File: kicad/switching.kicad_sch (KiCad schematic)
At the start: 7 parts

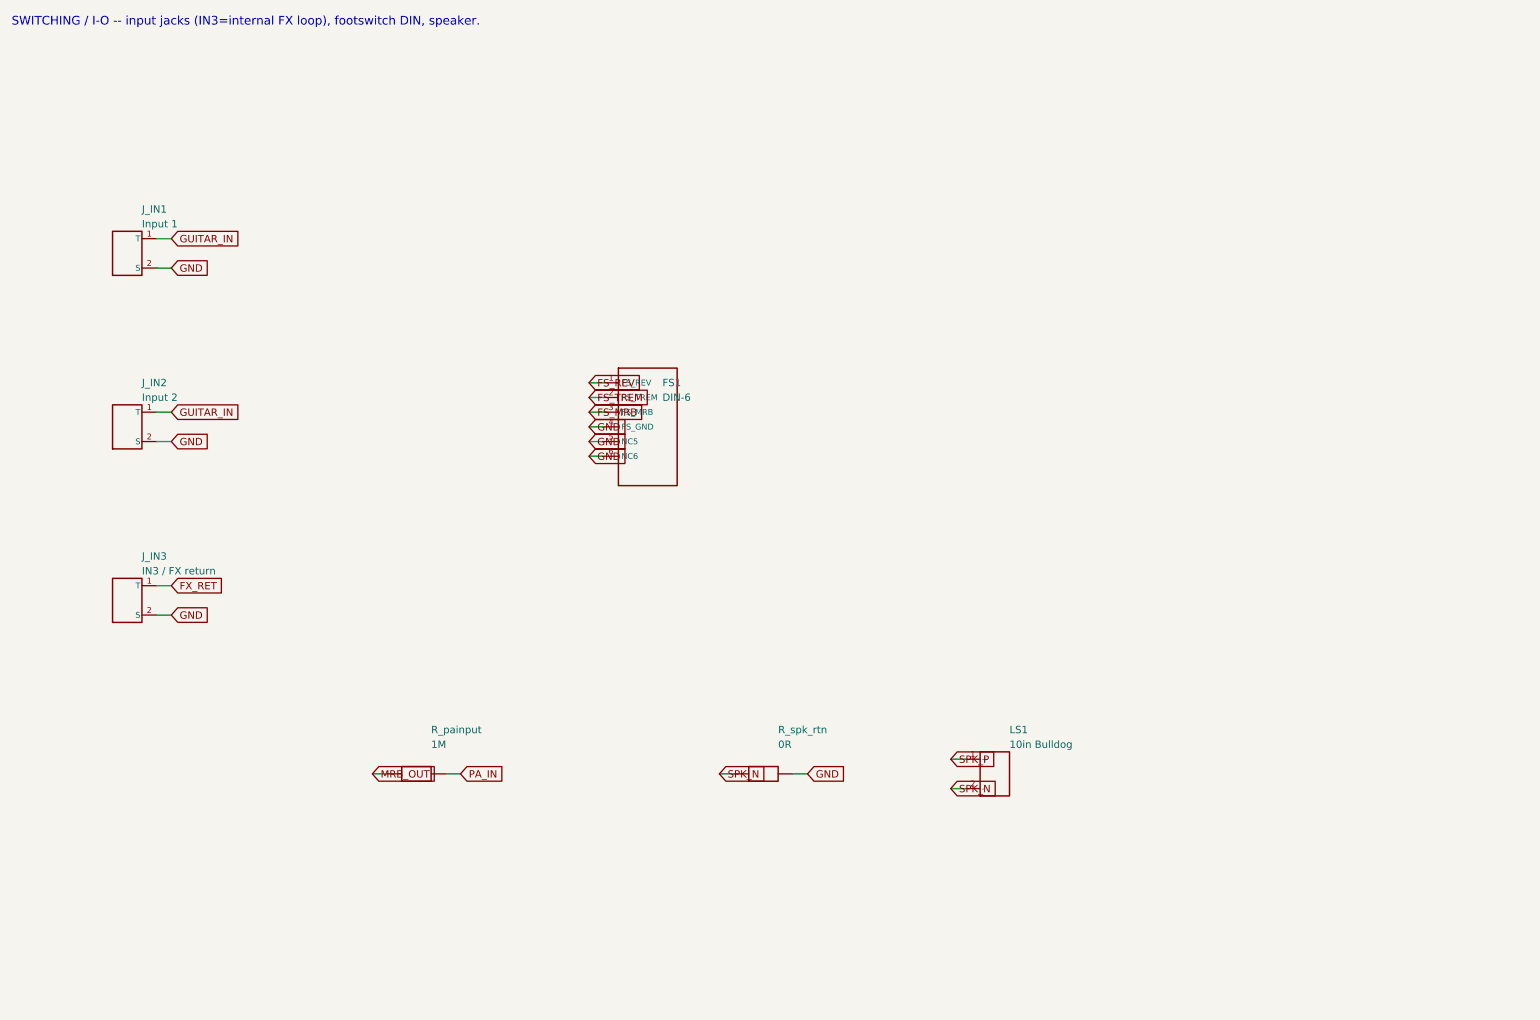
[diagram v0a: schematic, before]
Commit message: Schematic passes KiCad 8 ERC (0 violations); add op-amp mid-rail bias
Installed KiCad 8.0.9 and ran a real Electrical Rules Check on the generated
hierarchy. Drove it to 0 violations:
- snapped every pin/wire endpoint to the 1.27 mm connection grid (was 338
  endpoint_off_grid violations)
- gave the footswitch lines FS_REV/FS_TREM/FS_MRB a real second endpoint via
  100k control pulldowns on the reverb/tremolo/mrb sheets (was 3 dangling labels)

Also made the single-supply TL072 stages electrically real: added a mid-rail
VBIAS network (R_vb1/R_vb2 + C_vb on the Power Supply sheet) and referenced the
reverb driver and tremolo LFO inputs/gain-returns to VBIAS instead of GND
(design addition, flagged in the sheet notes).

Result: kicad-cli 8.0.9 sch erc -> 0 violations; netlist 102 components, 58
nets, 0 unconnected pins; VBIAS spans 10 nodes. Updated SCHEMATIC-BUILD.md,
kicad/README.md, CHANGELOG.md.

https://claude.ai/code/session_01PkrfUi9tvZfLvudJ7h23qD
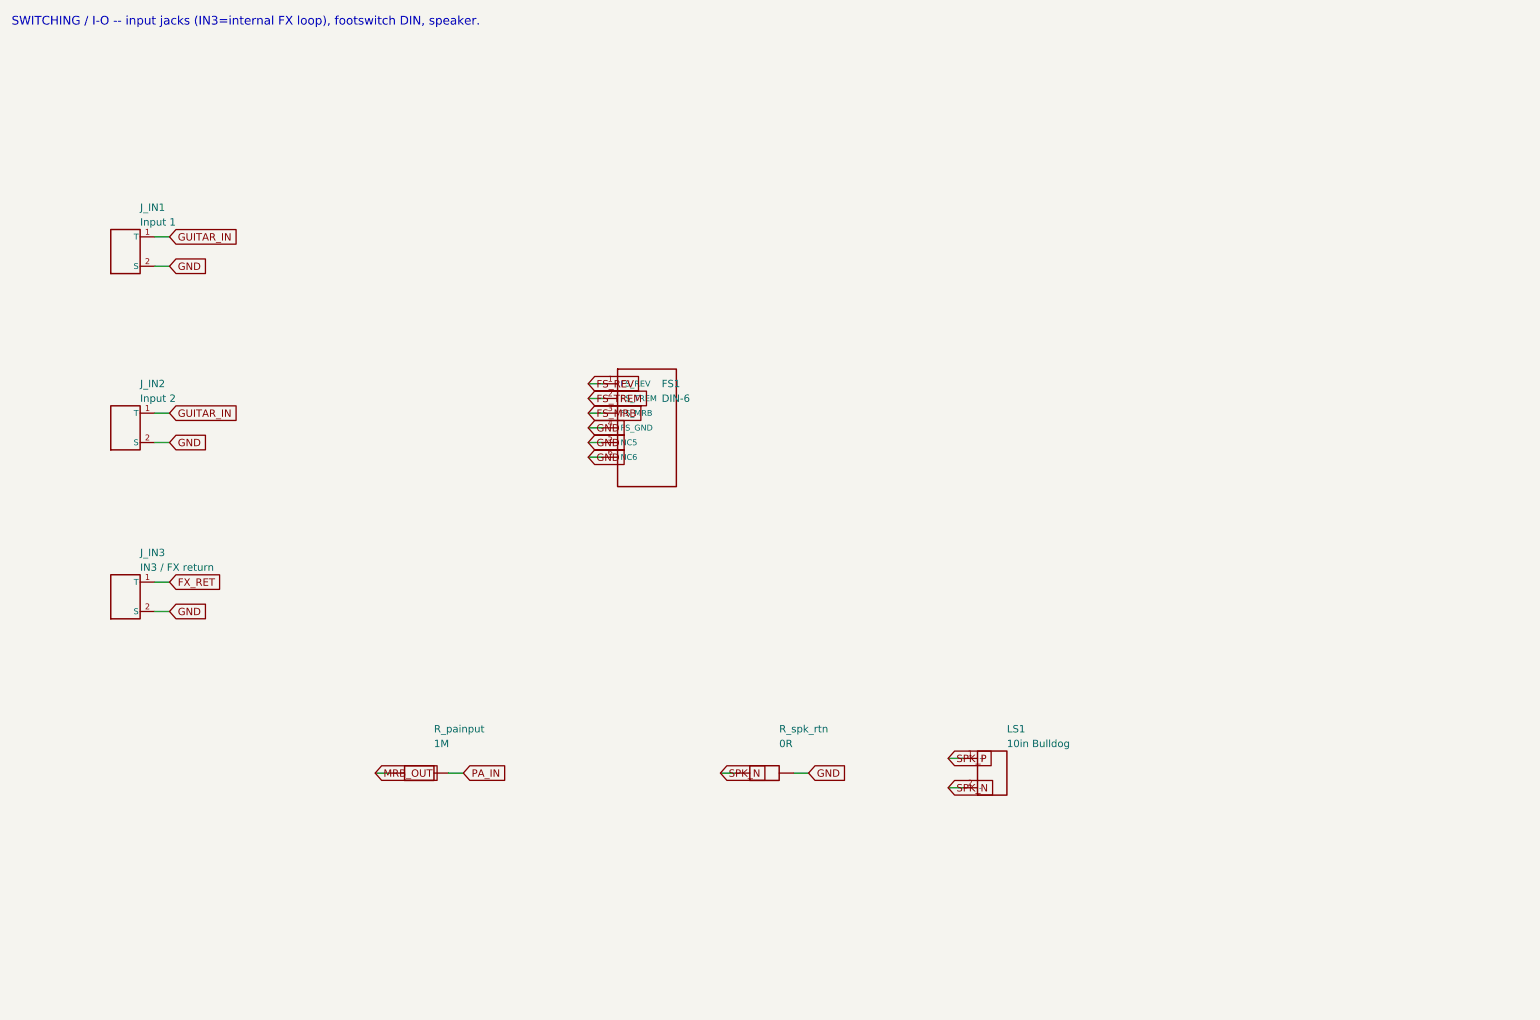
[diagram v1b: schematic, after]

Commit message: Generate auto-placed PCB (102 footprints, GND pour, board outline)
Build cambridge_reverb.kicad_pcb from the schematic via kicad/gen/gen_pcb.py
(KiCad 8 pcbnew API): assign a THT footprint to every component (standard libs
for generics + the project footprints for VTL5C1 and the 1H toroid), place all
102 footprints (off-board connectors on a bottom wiring-edge strip, toroid in a
reserved spot), assign all 58 nets to pads, draw a 190x115 mm Edge.Cuts outline,
and pour a bottom-layer GND plane. Footprint assignments also carry into the
schematic symbols.

The board opens in KiCad and the ratsnest matches the ERC-clean schematic. It is
placed but NOT routed: kicad-cli pcb drc is dominated by 130 unconnected
(unrouted signal nets; GND is poured) plus cosmetic silk/courtyard overlaps from
dense auto-placement at chassis size -- documented in kicad/PCB-NOTES.md with the
remaining hand-work (placement into floor-plan zones, routing, DRC-to-zero,
Gerbers). Net classes (Default/Power/HighCurrent) carry over for routing.

Also: schematic resistor footprint switched to the compact vertical variant;
gitignore DRC/ERC .rpt reports.

https://claude.ai/code/session_01PkrfUi9tvZfLvudJ7h23qD
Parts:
- FS1: footprint (none) -> Connector_PinHeader_2.54mm:PinHeader_1x06_P2.54mm_Vertical
- J_IN1, J_IN2, J_IN3, LS1: footprint (none) -> Connector_PinHeader_2.54mm:PinHeader_1x02_P2.54mm_Vertical
- R_painput, R_spk_rtn: footprint (none) -> Resistor_THT:R_Axial_DIN0207_L6.3mm_D2.5mm_P5.08mm_Vertical
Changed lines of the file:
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@@
     (property "Reference" "J_IN1" (at 62.23 52.07 0) (effects (font (size 1.27 1.27)) (justify left)))
     (property "Value" "Input 1" (at 62.23 54.61 0) (effects (font (size 1.27 1.27)) (justify left)))
-    (property "Footprint" "" (at 59.69 59.69 0) (effects (font (size 1.27 1.27)) hide))
+    (property "Footprint" "Connector_PinHeader_2.54mm:PinHeader_1x02_P2.54mm_Vertical" (at 59.69 59.69 0) (effects (font (size 1.27 1.27)) hide))
     (pin "1")
     (pin "2")
-    (instances (project "cambridge_reverb" (path "/ad5a9358-6f8c-4b19-a0b5-39da6586ee2a" (reference "J_IN1") (unit 1))))
+    (instances (project "cambridge_reverb" (path "/6a60d1d6-a2aa-4a66-856b-4be2c04fe058" (reference "J_IN1") (unit 1))))
   )
   (wire (pts (xy 64.77 57.15) (xy 67.31 57.15)) (stroke (width 0) (type default)))
@@
     (property "Reference" "J_IN2" (at 62.23 82.55 0) (effects (font (size 1.27 1.27)) (justify left)))
     (property "Value" "Input 2" (at 62.23 85.09 0) (effects (font (size 1.27 1.27)) (justify left)))
-    (property "Footprint" "" (at 59.69 90.17 0) (effects (font (size 1.27 1.27)) hide))
+    (property "Footprint" "Connector_PinHeader_2.54mm:PinHeader_1x02_P2.54mm_Vertical" (at 59.69 90.17 0) (effects (font (size 1.27 1.27)) hide))
     (pin "1")
     (pin "2")
-    (instances (project "cambridge_reverb" (path "/ad5a9358-6f8c-4b19-a0b5-39da6586ee2a" (reference "J_IN2") (unit 1))))
+    (instances (project "cambridge_reverb" (path "/6a60d1d6-a2aa-4a66-856b-4be2c04fe058" (reference "J_IN2") (unit 1))))
   )
   (wire (pts (xy 64.77 87.63) (xy 67.31 87.63)) (stroke (width 0) (type default)))
@@
     (property "Reference" "J_IN3" (at 62.23 111.75999999999999 0) (effects (font (size 1.27 1.27)) (justify left)))
     (property "Value" "IN3 / FX return" (at 62.23 114.3 0) (effects (font (size 1.27 1.27)) (justify left)))
-    (property "Footprint" "" (at 59.69 119.38 0) (effects (font (size 1.27 1.27)) hide))
+    (property "Footprint" "Connector_PinHeader_2.54mm:PinHeader_1x02_P2.54mm_Vertical" (at 59.69 119.38 0) (effects (font (size 1.27 1.27)) hide))
     (pin "1")
     (pin "2")
-    (instances (project "cambridge_reverb" (path "/ad5a9358-6f8c-4b19-a0b5-39da6586ee2a" (reference "J_IN3") (unit 1))))
+    (instances (project "cambridge_reverb" (path "/6a60d1d6-a2aa-4a66-856b-4be2c04fe058" (reference "J_IN3") (unit 1))))
   )
   (wire (pts (xy 64.77 116.83999999999999) (xy 67.31 116.83999999999999)) (stroke (width 0) (type default)))
@@
     (property "Reference" "FS1" (at 152.4 82.55 0) (effects (font (size 1.27 1.27)) (justify left)))
     (property "Value" "DIN-6" (at 152.4 85.09 0) (effects (font (size 1.27 1.27)) (justify left)))
-    (property "Footprint" "" (at 149.86 90.17 0) (effects (font (size 1.27 1.27)) hide))
+    (property "Footprint" "Connector_PinHeader_2.54mm:PinHeader_1x06_P2.54mm_Vertical" (at 149.86 90.17 0) (effects (font (size 1.27 1.27)) hide))
     (pin "1")
     (pin "2")
@@
     (pin "5")
     (pin "6")
-    (instances (project "cambridge_reverb" (path "/ad5a9358-6f8c-4b19-a0b5-39da6586ee2a" (reference "FS1") (unit 1))))
+    (instances (project "cambridge_reverb" (path "/6a60d1d6-a2aa-4a66-856b-4be2c04fe058" (reference "FS1") (unit 1))))
   )
   (wire (pts (xy 142.24 82.55) (xy 139.70000000000002 82.55)) (stroke (width 0) (type default)))
@@
     (property "Reference" "LS1" (at 212.09 142.24 0) (effects (font (size 1.27 1.27)) (justify left)))
     (property "Value" "10in Bulldog" (at 212.09 144.78 0) (effects (font (size 1.27 1.27)) (justify left)))
-    (property "Footprint" "" (at 209.55 149.86 0) (effects (font (size 1.27 1.27)) hide))
+    (property "Footprint" "Connector_PinHeader_2.54mm:PinHeader_1x02_P2.54mm_Vertical" (at 209.55 149.86 0) (effects (font (size 1.27 1.27)) hide))
     (pin "1")
     (pin "2")
-    (instances (project "cambridge_reverb" (path "/ad5a9358-6f8c-4b19-a0b5-39da6586ee2a" (reference "LS1") (unit 1))))
+    (instances (project "cambridge_reverb" (path "/6a60d1d6-a2aa-4a66-856b-4be2c04fe058" (reference "LS1") (unit 1))))
   )
   (wire (pts (xy 204.47 147.32000000000002) (xy 201.93 147.32000000000002)) (stroke (width 0) (type default)))
@@
     (property "Reference" "R_spk_rtn" (at 172.72 142.24 0) (effects (font (size 1.27 1.27)) (justify left)))
     (property "Value" "0R" (at 172.72 144.78 0) (effects (font (size 1.27 1.27)) (justify left)))
-    (property "Footprint" "" (at 170.18 149.86 0) (effects (font (size 1.27 1.27)) hide))
+    (property "Footprint" "Resistor_THT:R_Axial_DIN0207_L6.3mm_D2.5mm_P5.08mm_Vertical" (at 170.18 149.86 0) (effects (font (size 1.27 1.27)) hide))
     (pin "1")
     (pin "2")
-    (instances (project "cambridge_reverb" (path "/ad5a9358-6f8c-4b19-a0b5-39da6586ee2a" (reference "R_spk_rtn") (unit 1))))
+    (instances (project "cambridge_reverb" (path "/6a60d1d6-a2aa-4a66-856b-4be2c04fe058" (reference "R_spk_rtn") (unit 1))))
   )
   (wire (pts (xy 165.1 149.86) (xy 162.56 149.86)) (stroke (width 0) (type default)))
@@
     (property "Reference" "R_painput" (at 113.03 142.24 0) (effects (font (size 1.27 1.27)) (justify left)))
     (property "Value" "1M" (at 113.03 144.78 0) (effects (font (size 1.27 1.27)) (justify left)))
-    (property "Footprint" "" (at 110.49 149.86 0) (effects (font (size 1.27 1.27)) hide))
+    (property "Footprint" "Resistor_THT:R_Axial_DIN0207_L6.3mm_D2.5mm_P5.08mm_Vertical" (at 110.49 149.86 0) (effects (font (size 1.27 1.27)) hide))
     (pin "1")
     (pin "2")
-    (instances (project "cambridge_reverb" (path "/ad5a9358-6f8c-4b19-a0b5-39da6586ee2a" (reference "R_painput") (unit 1))))
+    (instances (project "cambridge_reverb" (path "/6a60d1d6-a2aa-4a66-856b-4be2c04fe058" (reference "R_painput") (unit 1))))
   )
   (wire (pts (xy 105.41 149.86) (xy 102.86999999999999 149.86)) (stroke (width 0) (type default)))

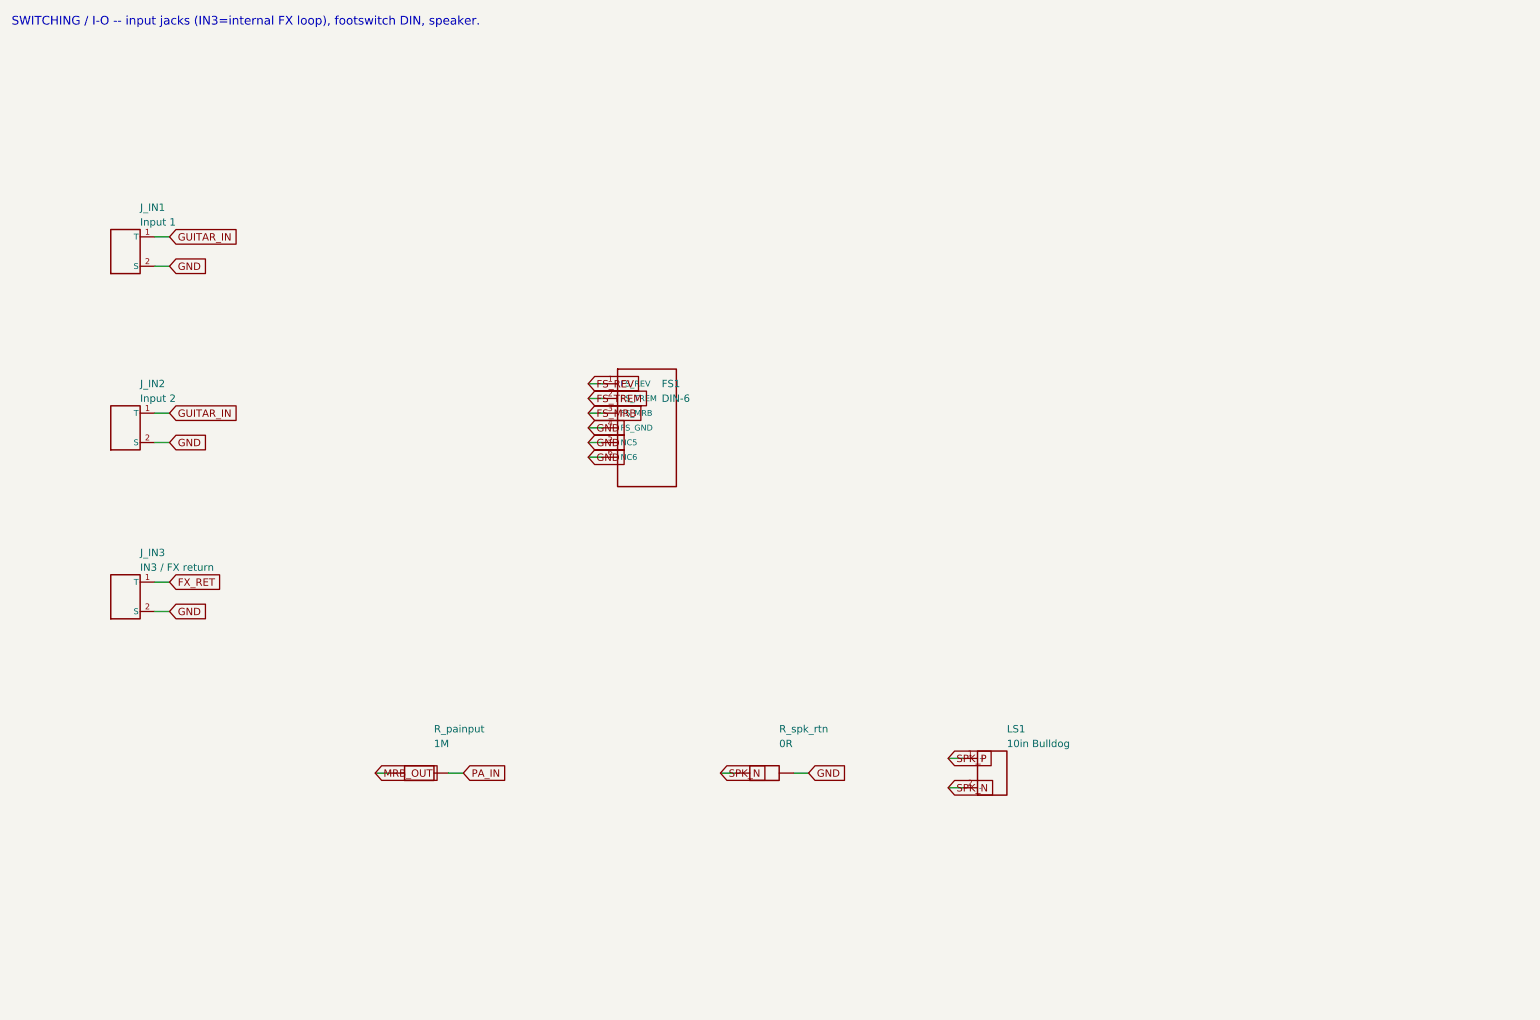
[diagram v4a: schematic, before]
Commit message: Audit pass: center schematic pages, PCB layout audit, SPICE audit
Schematic: gen_kicad.py now defers draw-op emission, computes each sheet's
content bounding box, and translates it to the page center (grid-snapped so pins
stay on the 1.27mm grid). All 8 sheets are centered on the page instead of
crammed top-left; ERC still 0 violations.

PCB: full category-by-category audit in kicad/PCB-AUDIT.md (footprints,
placement, net classes, copper/GND, routing) with prioritized fixes. Applied:
- the 5 reused/off-board pots were modeled with a 16mm panel-pot footprint; they
  are panel-mounted (wired off-board), so they're now 3-pad wiring connectors --
  more correct and a big silk-overlap source removed (packing 51%->48%)
- centered the component grid
Documented findings: LM1875 TO-220-5 annular is 0.0875mm (1.275mm pad on 1.1mm
drill) vs the 0.15mm rule; KBP410G bridge uses a placeholder header footprint;
silk/courtyard overlaps are a density symptom (the 82% packing on the 155x90
safe-bet). Non-routing DRC errors: 9; demo board still 0.

SPICE: audited every netlist/model (spice/README.md). All five run under
ngspice-42 (exit 0) and match the documented numbers; no correctness issues.

https://claude.ai/code/session_01PkrfUi9tvZfLvudJ7h23qD
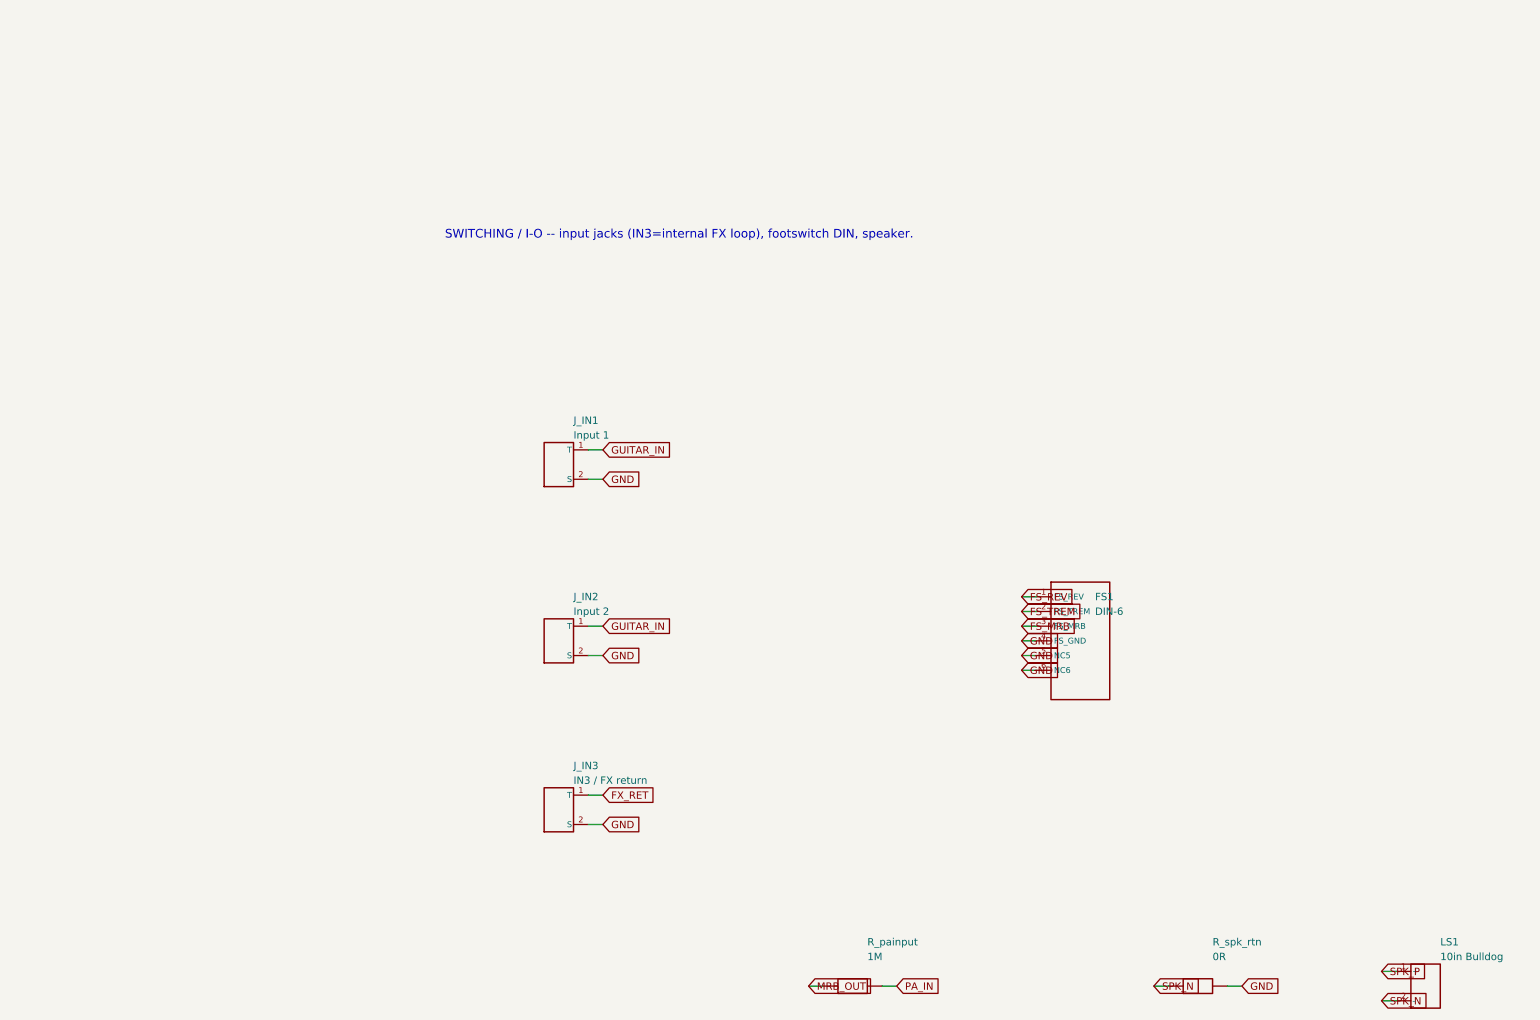
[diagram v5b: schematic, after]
